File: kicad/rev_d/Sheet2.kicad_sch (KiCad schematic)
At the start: 168 parts, among them J10 vg_old, J5 external clock, J6 JUMPER, J8 JUMPER, J9 JUMPER, Q2 QUARTZ, Q3 QUARTZ32768, U2 PCA9555DB, X11 KEYB-MOUSE, X12 IDC20, X13 USB_C, X15 PLB2-2, X19 AVR pgm conn, X4 IDC10M, X5 IDC10M, X6 RS232_9

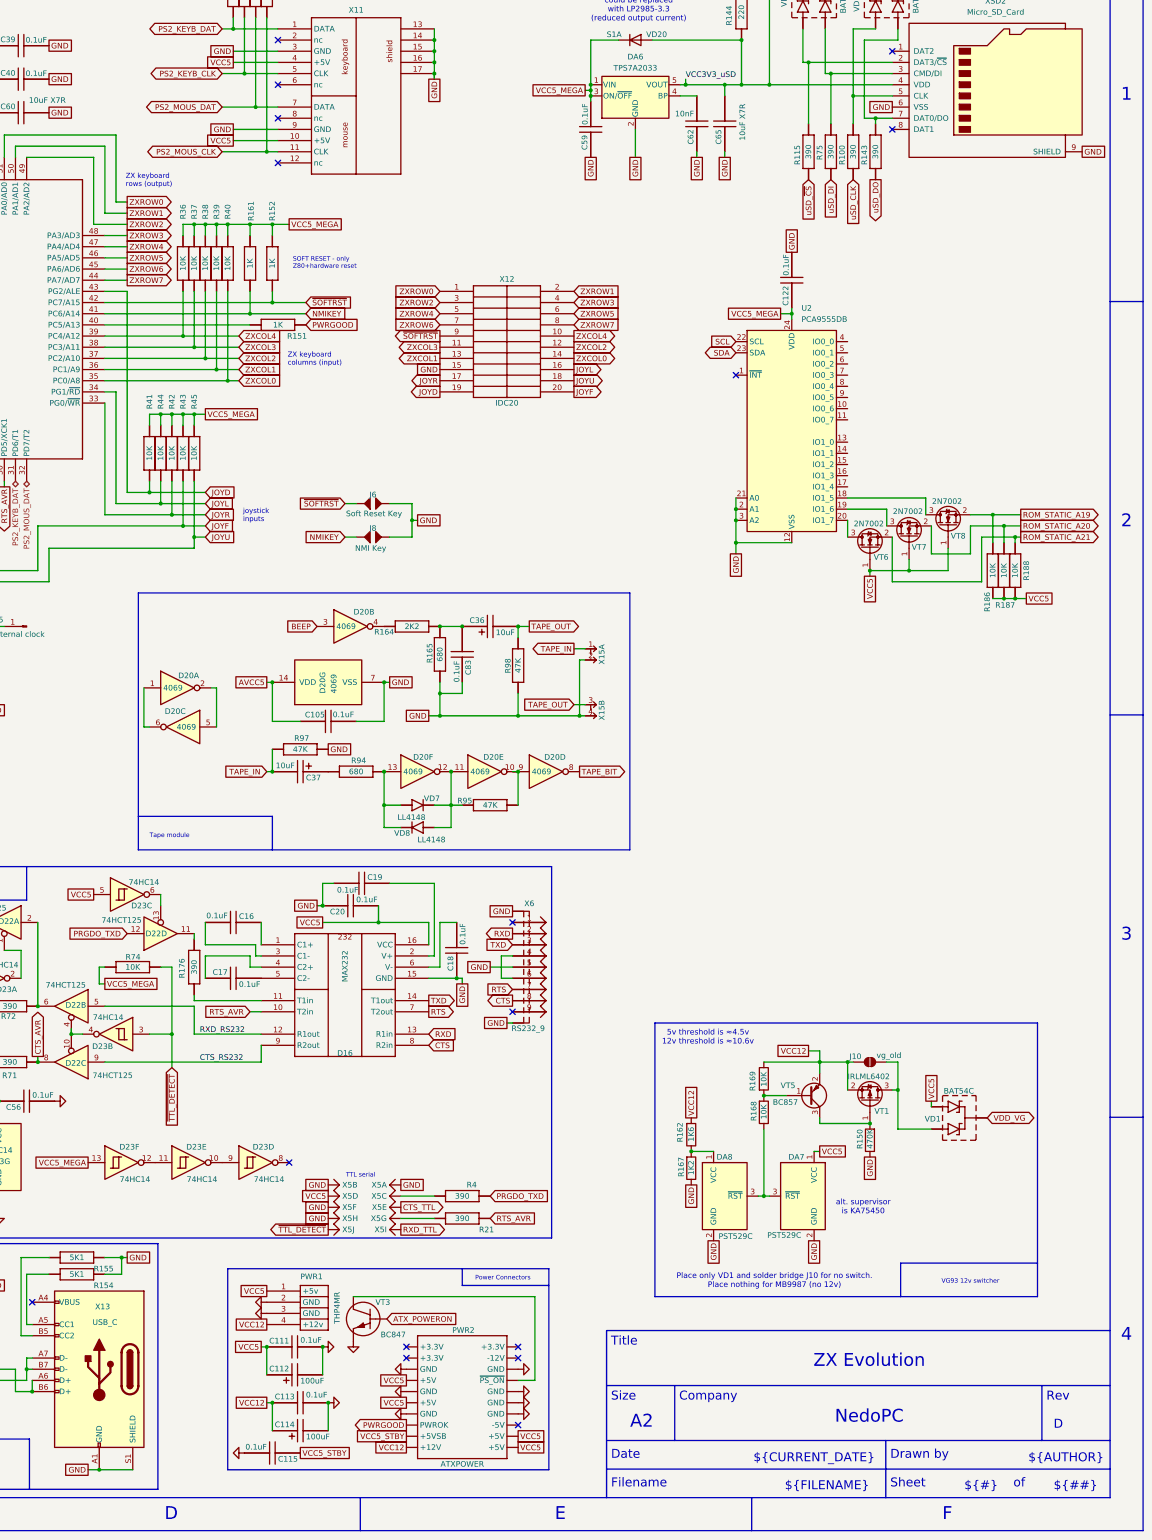
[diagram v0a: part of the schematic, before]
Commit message: pentevo: rev D: add SHIELD net, connect DB-xx shields, sdcard shields and mounting holes there
git-svn-id: svn://localhost/local-pentevo@1259 c6c76956-fad2-4150-a3a9-ea0a427205ba
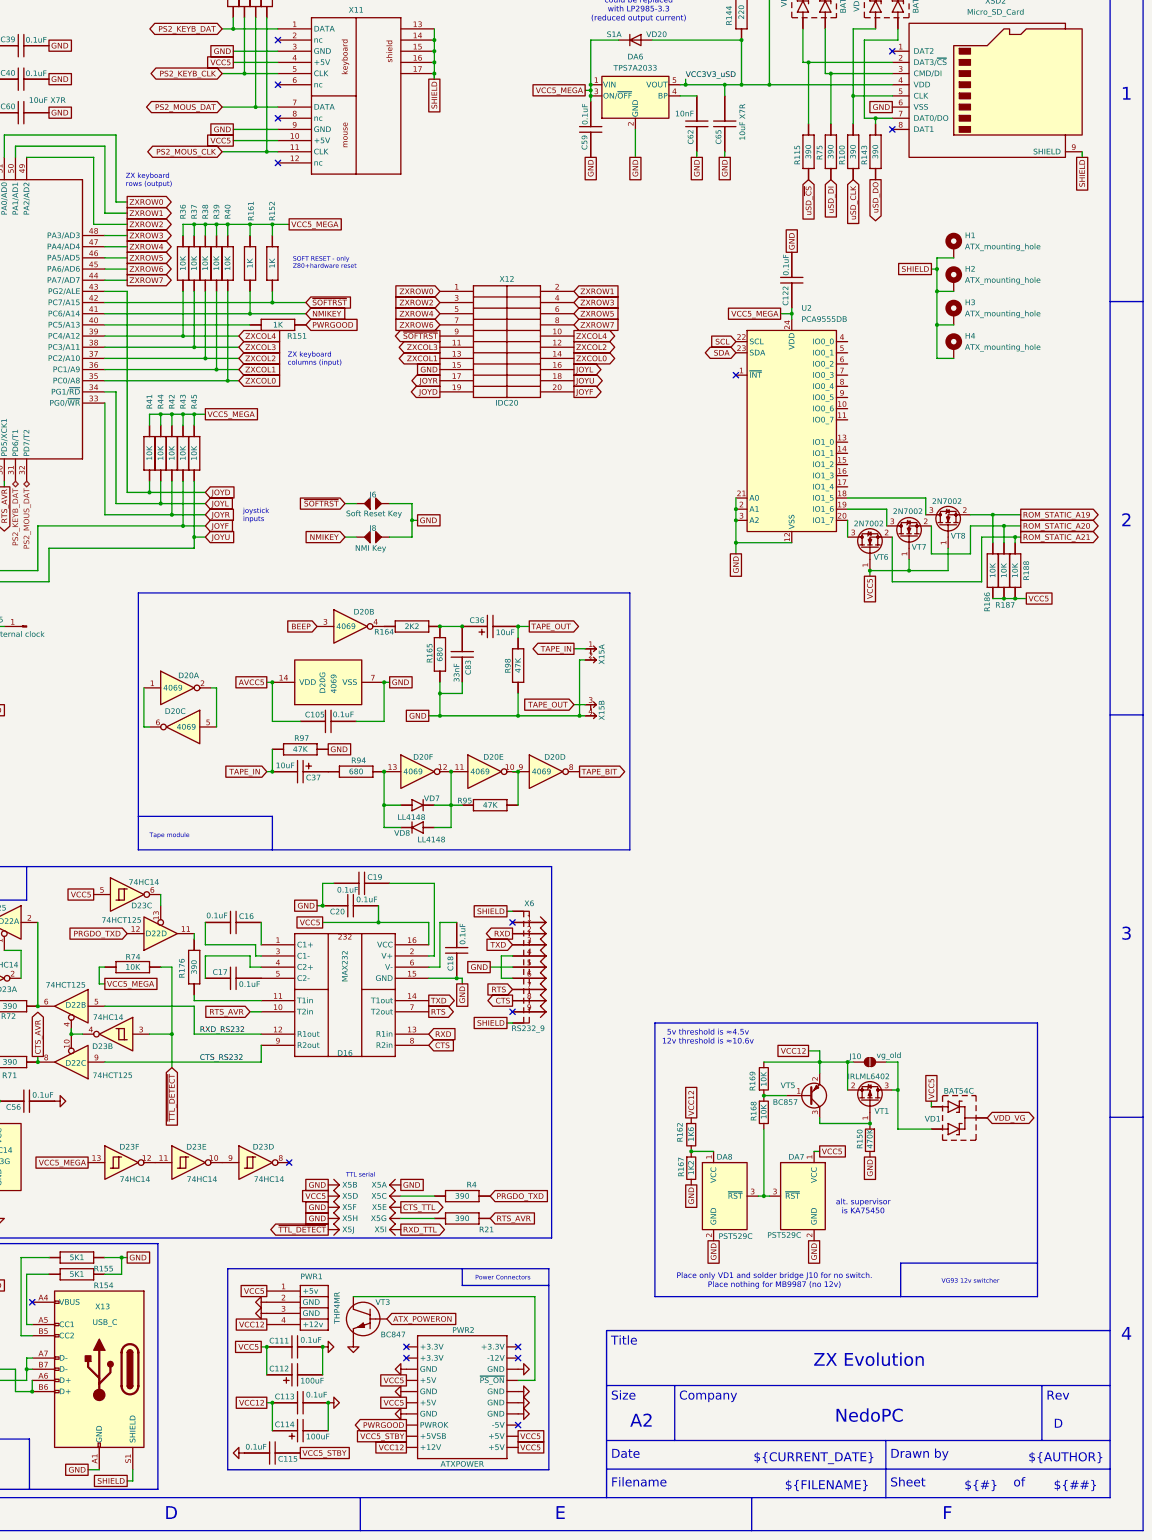
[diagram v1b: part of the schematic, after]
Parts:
- added H1, H2, H3, H4: ATX_mounting_hole, symbol Mechanical:MountingHole_Pad
- C83: value 0.1uF -> 33nF
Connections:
- net GND: no longer X11.13 (shield), X11.14 (shield), X11.15 (shield), X11.16 (shield), X11.17 (shield), X13.S1 (SHIELD), X6.10, X6.11, XSD2.9 (SHIELD)
- new net SHIELD: H1.1, H2.1, H3.1, H4.1, X11.13 (shield), X11.14 (shield), X11.15 (shield), X11.16 (shield), X11.17 (shield), X13.S1 (SHIELD), X6.10, X6.11, XSD2.9 (SHIELD)

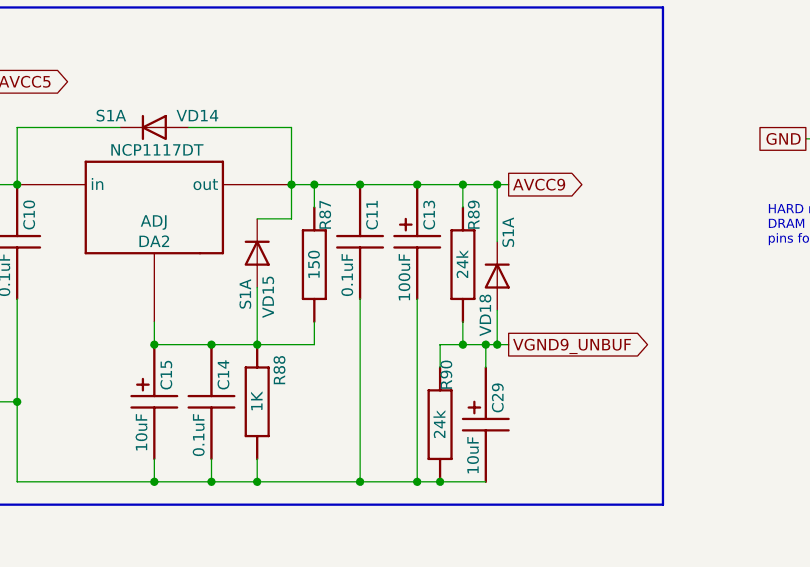
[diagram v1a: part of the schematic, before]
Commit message: pentevo: rev D: remove output 100uF cap for AVCC9, 10uF instead
git-svn-id: svn://localhost/local-pentevo@1260 c6c76956-fad2-4150-a3a9-ea0a427205ba
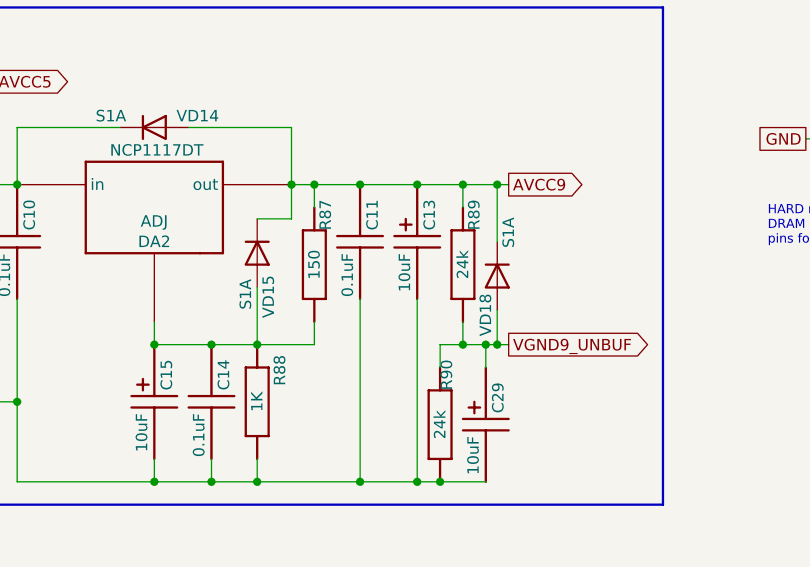
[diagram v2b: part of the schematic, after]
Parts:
- removed C13: 100uF, EC-CHIPB, symbol eva-altium-import:Sheet2_3_ECAPCHIPB
- added C13: 10uF, EC-CHIP, symbol eva-altium-import:Sheet2_3_ECAPCHIP
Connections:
- net AVCC9: now also C13.1
- net GND: now also C13.2
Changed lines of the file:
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@@
 	)
 	(junction
-		(at 175.26 218.44)
-		(diameter 0)
-		(color 0 0 0 0)
-	)
-	(junction
 		(at 337.82 121.92)
 		(diameter 0)
@@
 	)
 	(junction
+		(at 175.26 218.44)
+		(diameter 0)
+		(color 0 0 0 0)
+	)
+	(junction
 		(at 420.37 90.17)
 		(diameter 0)
@@
 	(wire
 		(pts
-			(xy 168.91 218.44) (xy 175.26 218.44)
-		)
-		(stroke
-			(width 0)
-			(type default)
-		)
-	)
-	(wire
-		(pts
 			(xy 127 218.44) (xy 130.81 218.44)
 		)
@@
 	(wire
 		(pts
+			(xy 175.26 218.44) (xy 180.34 218.44)
+		)
+		(stroke
+			(width 0)
+			(type default)
+		)
+	)
+	(wire
+		(pts
 			(xy 514.35 207.01) (xy 516.89 207.01)
 		)
@@
 	(wire
 		(pts
-			(xy 175.26 218.44) (xy 180.34 218.44)
+			(xy 168.91 218.44) (xy 175.26 218.44)
 		)
 		(stroke
@@
 	)
 	(symbol
+		(lib_id "eva-altium-import:Sheet2_3_ECAPCHIP")
+		(at 175.26 218.44 0)
+		(unit 1)
+		(exclude_from_sim no)
+		(in_bom yes)
+		(on_board yes)
+		(dnp no)
+		(property "Reference" "C13"
+			(at 175.895 223.52 90)
+			(effects
+				(font
+					(size 1.27 1.27)
+				)
+				(justify left top)
+			)
+		)
+		(property "Value" "10uF"
+			(at 174.625 226.06 90)
+			(effects
+				(font
+					(size 1.27 1.27)
+				)
+				(justify right bottom)
+			)
+		)
+		(property "Footprint" "EC-CHIP"
+			(at 175.26 218.44 0)
+			(effects
+				(font
+					(size 1.27 1.27)
+				)
+				(hide yes)
+			)
+		)
+		(property "Datasheet" ""
+			(at 175.26 218.44 0)
+			(effects
+				(font
+					(size 1.27 1.27)
+				)
+				(hide yes)
+			)
+		)
+		(property "Description" "ECAPCHIP"
+			(at 175.26 218.44 0)
+			(effects
+				(font
+					(size 1.27 1.27)
+				)
+				(hide yes)
+			)
+		)
+		(pin "1"
+		)
+		(pin "2"
+		)
+		(instances
+			(project "eva"
+				(path "/ab605654-a730-497b-9e09-9b351f74b935/31d5864f-06ec-4c73-9256-780a6880087d"
+					(reference "C13")
+					(unit 1)
+				)
+			)
+		)
+	)
+	(symbol
 		(lib_id "74xx:74HC14")
 		(at 344.17 335.28 0)
@@
 					(unit 1)
 				)
-			)
-		)
-	)
-	(symbol
-		(lib_id "eva-altium-import:Sheet2_3_ECAPCHIPB")
-		(at 175.26 218.44 0)
-		(unit 1)
-		(exclude_from_sim no)
-		(in_bom yes)
-		(on_board yes)
-		(dnp no)
-		(property "Reference" "C13"
-			(at 175.895 223.52 90)
-			(effects
-				(font
-					(size 1.27 1.27)
-				)
-				(justify left top)
-			)
-		)
-		(property "Value" "100uF"
-			(at 174.625 226.06 90)
-			(effects
-				(font
-					(size 1.27 1.27)
-				)
-				(justify right bottom)
-			)
-		)
-		(property "Footprint" "EC-CHIPB"
-			(at 175.26 218.44 0)
-			(effects
-				(font
-					(size 1.27 1.27)
-				)
-				(hide yes)
-			)
-		)
-		(property "Datasheet" ""
-			(at 175.26 218.44 0)
-			(effects
-				(font
-					(size 1.27 1.27)
-				)
-				(hide yes)
-			)
-		)
-		(property "Description" "ECAPCHIPB"
-			(at 175.26 218.44 0)
-			(effects
-				(font
-					(size 1.27 1.27)
-				)
-				(hide yes)
-			)
-		)
-		(pin "4"
-		)
-		(pin "3"
-		)
-		(pin "1"
-		)
-		(pin "2"
-		)
-		(instances
-			(project ""
-				(path "/ab605654-a730-497b-9e09-9b351f74b935/31d5864f-06ec-4c73-9256-780a6880087d"
-					(reference "C13")
-					(unit 1)
-				)

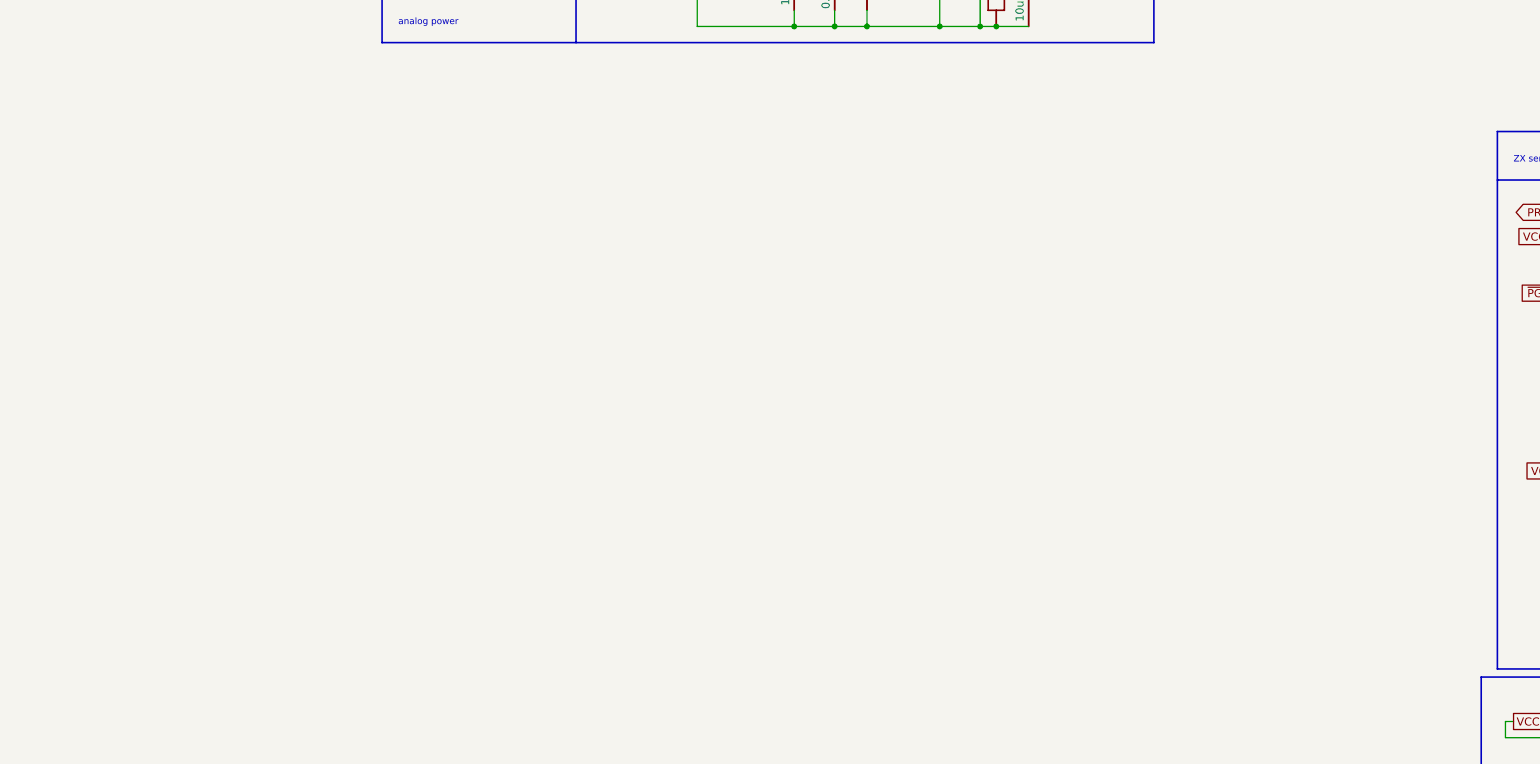
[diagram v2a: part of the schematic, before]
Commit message: pentevo: rev D: add TSOP DRAM to schematics
git-svn-id: svn://localhost/local-pentevo@1263 c6c76956-fad2-4150-a3a9-ea0a427205ba
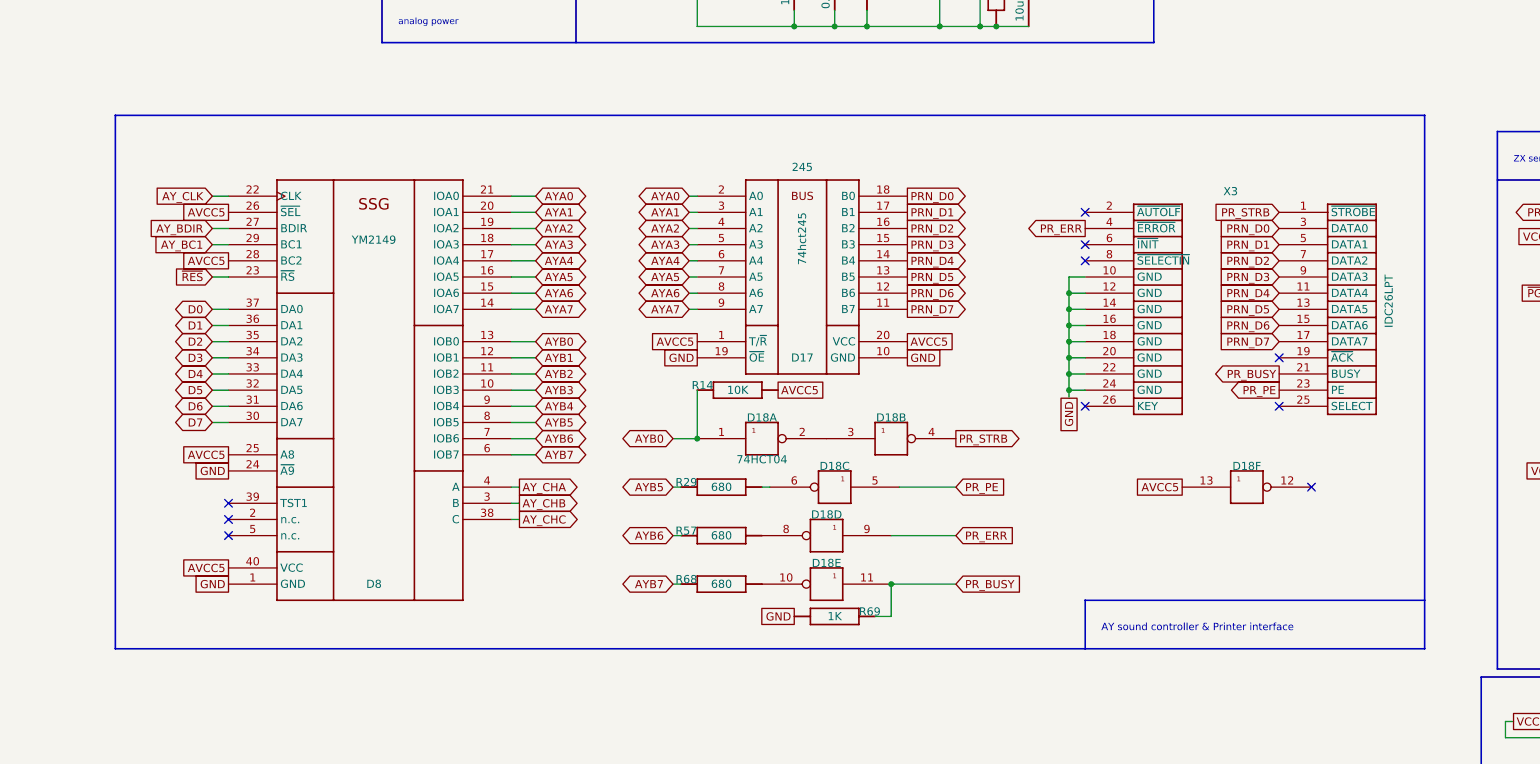
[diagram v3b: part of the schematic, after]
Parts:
- added D17: 245, Package_SO:TSSOP-20_4.4x6.5mm_P0.65mm, symbol eva-altium-import:Sheet1_0_245
- added D18: 04, SO14, symbol eva-altium-import:Sheet1_0_mirrored_04
- added D8: YM2149, DIP40, symbol eva-altium-import:Sheet1_0_YM2149
- added R14: 10K, R-CHIP, symbol eva-altium-import:Sheet1_0_RESCHIP
- added R29, R57, R68: 680, R-CHIP, symbol eva-altium-import:Sheet1_0_RESCHIP
- added R69: 1K, R-CHIP, symbol eva-altium-import:Sheet1_0_mirrored_RESCHIP
- added X3: IDC26LPT, IDC26, symbol eva-altium-import:Sheet1_0_mirrored_IDC26LPT
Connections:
- net AVCC5: now also D17.1 (T/~{R}), D17.20 (VCC), D18.13, D8.25 (A8), D8.26 (~{SEL}), D8.28 (BC2), D8.40 (VCC), R14.1 (i/o)
- net GND: now also D17.10 (GND), D17.19 (~{OE}), D18.6, D18.7 (GND), D18.7 (GND), D18.7 (GND), D18.7 (GND), D18.7 (GND), D18.7 (GND), D8.1 (GND), D8.24 (~{A9}), R29.1 (i/o), R69.1 (i/o), X3.10 (GND), X3.12 (GND), X3.14 (GND), X3.16 (GND), X3.18 (GND), X3.20 (GND), X3.22 (GND), X3.24 (GND)
- new net: D18.10, R68.1 (i/o)
- new net: D18.2, D18.3
- new net: D18.8, R57.1 (i/o)
- new net +5v: D18.14 (+5v), D18.14 (+5v), D18.14 (+5v), D18.14 (+5v), D18.14 (+5v), D18.14 (+5v)
- new net AYA0: D17.2 (A0), D8.21 (IOA0)
- new net AYA1: D17.3 (A1), D8.20 (IOA1)
- new net AYA2: D17.4 (A2), D8.19 (IOA2)
- new net AYA3: D17.5 (A3), D8.18 (IOA3)
- new net AYA4: D17.6 (A4), D8.17 (IOA4)
- new net AYA5: D17.7 (A5), D8.16 (IOA5)
- new net AYA6: D17.8 (A6), D8.15 (IOA6)
- new net AYA7: D17.9 (A7), D8.14 (IOA7)
- new net AYB0: D18.1, D8.13 (IOB0), R14.2 (i/o1)
- new net AYB1: D8.12 (IOB1)
- new net AYB2: D8.11 (IOB2)
- new net AYB3: D8.10 (IOB3)
- new net AYB4: D8.9 (IOB4)
- new net AYB5: D8.8 (IOB5), R29.2 (i/o1)
- new net AYB6: D8.7 (IOB6), R57.2 (i/o1)
- new net AYB7: D8.6 (IOB7), R68.2 (i/o1)
- new net AY_BC1: D8.29 (BC1)
- new net AY_BDIR: D8.27 (BDIR)
- new net AY_CHA: D8.4 (A)
- new net AY_CHB: D8.3 (B)
- new net AY_CHC: D8.38 (C)
- new net AY_CLK: D8.22 (CLK)
- new net D0: D8.37 (DA0)
- new net D1: D8.36 (DA1)
- new net D2: D8.35 (DA2)
- new net D3: D8.34 (DA3)
- new net D4: D8.33 (DA4)
- new net D5: D8.32 (DA5)
- new net D6: D8.31 (DA6)
- new net D7: D8.30 (DA7)
- new net PRN_D0: D17.18 (B0), X3.3 (DATA0)
- new net PRN_D1: D17.17 (B1), X3.5 (DATA1)
- new net PRN_D2: D17.16 (B2), X3.7 (DATA2)
- new net PRN_D3: D17.15 (B3), X3.9 (DATA3)
- new net PRN_D4: D17.14 (B4), X3.11 (DATA4)
- new net PRN_D5: D17.13 (B5), X3.13 (DATA5)
- new net PRN_D6: D17.12 (B6), X3.15 (DATA6)
- new net PRN_D7: D17.11 (B7), X3.17 (DATA7)
- new net PR_BUSY: D18.11, R69.2 (i/o1), X3.21 (BUSY)
- new net PR_ERR: D18.9, X3.4 (~{ERROR})
- new net PR_PE: D18.5, X3.23 (PE)
- new net PR_STRB: D18.4, X3.1 (~{STROBE})
- new net ~{RES}: D8.23 (~{RS})
- no-connect marks 23 -> 33
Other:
- note added: "AY sound controller & Printer interface"
